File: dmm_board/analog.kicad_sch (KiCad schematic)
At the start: 8 parts

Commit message: work with input prot
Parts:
- removed NT?: NetTie_2, symbol Device:NetTie_2
- added J?: Conn_01x04, symbol Connector_Generic:Conn_01x04
- added NT?: NetTie_2, symbol Device:NetTie_2
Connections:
- net GND: now also C?.2, C?.2, C?.2, NT?.1
- net GNDA: now also NT?.2
- no-connect marks 0 -> 6
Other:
- added sheet current_input (current_input.kicad_sch)
- note added: "v+ mA/uA A com"
- moved on the sheet: C?, U?

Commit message: stuff
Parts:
- added C?: 100n, Capacitor_SMD:C_0603_1608Metric_Pad1.08x0.95mm_HandSolder, symbol Device:C
- added U?: MAX4239AUT, Package_TO_SOT_SMD:SOT-23-6, symbol Amplifier_Operational:MAX4239AUT
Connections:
- new net +2V5: C?.1, U?.5 (~{SHDN}), U?.6 (V+)
- new net -2V5: C?.2
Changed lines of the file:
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@@
   (junction (at 193.04 47.625) (diameter 0) (color 0 0 0 0)
   )
+  (junction (at 123.19 92.075) (diameter 0) (color 0 0 0 0)
+  )
   (junction (at 236.22 47.625) (diameter 0) (color 0 0 0 0)
+  )
+  (junction (at 123.19 82.55) (diameter 0) (color 0 0 0 0)
   )
   (no_connect (at 238.125 65.405))
@@
     (stroke (width 0) (type default) (color 0 0 0 0))
   )
+  (wire (pts (xy 125.73 108.585) (xy 145.415 108.585))
+    (stroke (width 0) (type default) (color 0 0 0 0))
+  )
+  (wire (pts (xy 123.19 82.55) (xy 123.19 92.075))
+    (stroke (width 0) (type default) (color 0 0 0 0))
+  )
   (wire (pts (xy 222.885 102.87) (xy 222.885 100.965))
     (stroke (width 0) (type default) (color 0 0 0 0))
@@
     (stroke (width 0) (type default) (color 0 0 0 0))
   )
+  (wire (pts (xy 145.415 92.075) (xy 123.19 92.075))
+    (stroke (width 0) (type default) (color 0 0 0 0))
+  )
   (wire (pts (xy 193.04 47.625) (xy 193.04 48.26))
     (stroke (width 0) (type default) (color 0 0 0 0))
@@
     (stroke (width 0) (type default) (color 0 0 0 0))
   )
+  (wire (pts (xy 114.3 82.55) (xy 123.19 82.55))
+    (stroke (width 0) (type default) (color 0 0 0 0))
+  )
+  (wire (pts (xy 114.3 83.185) (xy 114.3 82.55))
+    (stroke (width 0) (type default) (color 0 0 0 0))
+  )
   (wire (pts (xy 227.33 38.1) (xy 227.33 39.37))
     (stroke (width 0) (type default) (color 0 0 0 0))
@@
     (stroke (width 0) (type default) (color 0 0 0 0))
   )
+  (wire (pts (xy 123.19 92.075) (xy 123.19 93.345))
+    (stroke (width 0) (type default) (color 0 0 0 0))
+  )
   (wire (pts (xy 203.2 38.1) (xy 212.09 38.1))
     (stroke (width 0) (type default) (color 0 0 0 0))
@@
     (stroke (width 0) (type default) (color 0 0 0 0))
   )
+  (wire (pts (xy 114.3 92.075) (xy 114.3 90.805))
+    (stroke (width 0) (type default) (color 0 0 0 0))
+  )
   (wire (pts (xy 212.09 46.99) (xy 212.09 47.625))
     (stroke (width 0) (type default) (color 0 0 0 0))
@@
     (stroke (width 0) (type default) (color 0 0 0 0))
   )
+  (wire (pts (xy 123.19 81.915) (xy 123.19 82.55))
+    (stroke (width 0) (type default) (color 0 0 0 0))
+  )
   (wire (pts (xy 227.33 47.625) (xy 227.33 46.99))
     (stroke (width 0) (type default) (color 0 0 0 0))
@@
   )
   (wire (pts (xy 222.885 81.915) (xy 222.885 88.9))
+    (stroke (width 0) (type default) (color 0 0 0 0))
+  )
+  (wire (pts (xy 145.415 108.585) (xy 145.415 92.075))
     (stroke (width 0) (type default) (color 0 0 0 0))
   )
@@
     )
     (property "Datasheet" "" (id 3) (at 217.805 88.9 0)
+      (effects (font (size 1.27 1.27)) hide)
+    )
+    (pin "1")
+  )
+  (symbol (lib_id "power:-2V5") (at 114.3 92.075 180) (unit 1)
+    (in_bom yes) (on_board yes) (fields_autoplaced)
+    (property "Reference" "#PWR?" (id 0) (at 114.3 94.615 0)
+      (effects (font (size 1.27 1.27)) hide)
+    )
+    (property "Value" "-2V5" (id 1) (at 115.697 93.824 0)
+      (effects (font (size 1.27 1.27)) (justify right))
+    )
+    (property "Footprint" "" (id 2) (at 114.3 92.075 0)
+      (effects (font (size 1.27 1.27)) hide)
+    )
+    (property "Datasheet" "" (id 3) (at 114.3 92.075 0)
       (effects (font (size 1.27 1.27)) hide)
     )
@@
     (pin "1")
   )
+  (symbol (lib_id "power:-2V5") (at 123.19 112.395 180) (unit 1)
+    (in_bom yes) (on_board yes) (fields_autoplaced)
+    (property "Reference" "#PWR?" (id 0) (at 123.19 114.935 0)
+      (effects (font (size 1.27 1.27)) hide)
+    )
+    (property "Value" "-2V5" (id 1) (at 124.587 114.144 0)
+      (effects (font (size 1.27 1.27)) (justify right))
+    )
+    (property "Footprint" "" (id 2) (at 123.19 112.395 0)
+      (effects (font (size 1.27 1.27)) hide)
+    )
+    (property "Datasheet" "" (id 3) (at 123.19 112.395 0)
+      (effects (font (size 1.27 1.27)) hide)
+    )
+    (pin "1")
+  )
   (symbol (lib_id "Device:C") (at 244.475 43.18 0) (unit 1)
     (in_bom yes) (on_board yes) (fields_autoplaced)
@@
     )
     (property "Datasheet" "" (id 3) (at 222.885 102.87 0)
+      (effects (font (size 1.27 1.27)) hide)
+    )
+    (pin "1")
+  )
+  (symbol (lib_id "power:+2V5") (at 123.19 81.915 0) (unit 1)
+    (in_bom yes) (on_board yes) (fields_autoplaced)
+    (property "Reference" "#PWR?" (id 0) (at 123.19 85.725 0)
+      (effects (font (size 1.27 1.27)) hide)
+    )
+    (property "Value" "+2V5" (id 1) (at 123.19 78.3105 0))
+    (property "Footprint" "" (id 2) (at 123.19 81.915 0)
+      (effects (font (size 1.27 1.27)) hide)
+    )
+    (property "Datasheet" "" (id 3) (at 123.19 81.915 0)
       (effects (font (size 1.27 1.27)) hide)
     )
@@
     (pin "2")
   )
+  (symbol (lib_id "Device:C") (at 114.3 86.995 0) (unit 1)
+    (in_bom yes) (on_board yes) (fields_autoplaced)
+    (property "Reference" "C?" (id 0) (at 117.221 86.0865 0)
+      (effects (font (size 1.27 1.27)) (justify left))
+    )
+    (property "Value" "100n" (id 1) (at 117.221 88.8616 0)
+      (effects (font (size 1.27 1.27)) (justify left))
+    )
+    (property "Footprint" "Capacitor_SMD:C_0603_1608Metric_Pad1.08x0.95mm_HandSolder" (id 2) (at 115.2652 90.805 0)
+      (effects (font (size 1.27 1.27)) hide)
+    )
+    (property "Datasheet" "~" (id 3) (at 114.3 86.995 0)
+      (effects (font (size 1.27 1.27)) hide)
+    )
+    (pin "1")
+    (pin "2")
+  )
   (symbol (lib_id "power:GND") (at 193.04 48.26 0) (unit 1)
     (in_bom yes) (on_board yes) (fields_autoplaced)
@@
     (pin "2")
   )
+  (symbol (lib_id "Amplifier_Operational:MAX4239AUT") (at 125.73 100.965 0) (unit 1)
+    (in_bom yes) (on_board yes) (fields_autoplaced)
+    (property "Reference" "U?" (id 0) (at 137.6385 96.8715 0))
+    (property "Value" "MAX4239AUT" (id 1) (at 137.6385 99.6466 0))
+    (property "Footprint" "Package_TO_SOT_SMD:SOT-23-6" (id 2) (at 125.73 100.965 0)
+      (effects (font (size 1.27 1.27)) hide)
+    )
+    (property "Datasheet" "http://datasheets.maximintegrated.com/en/ds/MAX4238-MAX4239.pdf" (id 3) (at 129.54 97.155 0)
+      (effects (font (size 1.27 1.27)) hide)
+    )
+    (pin "1")
+    (pin "2")
+    (pin "3")
+    (pin "4")
+    (pin "5")
+    (pin "6")
+  )
   (symbol (lib_id "Device:C") (at 203.2 43.18 0) (unit 1)

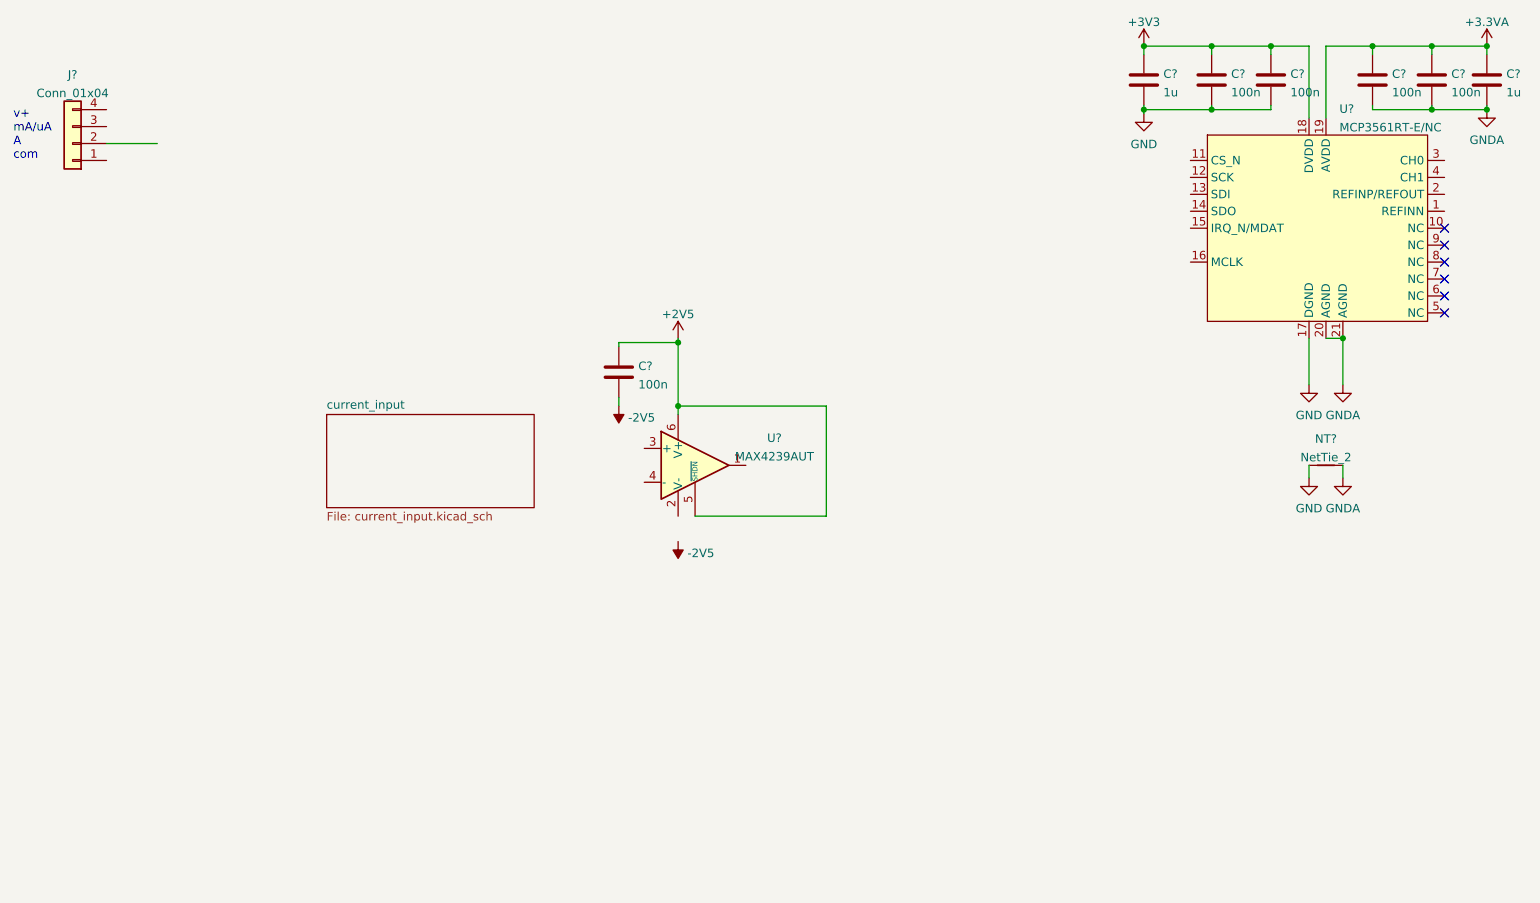
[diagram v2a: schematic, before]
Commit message: more analog input work
need new amp for current -8 instead of -9 that
-8 is unity gain stable -9 is not
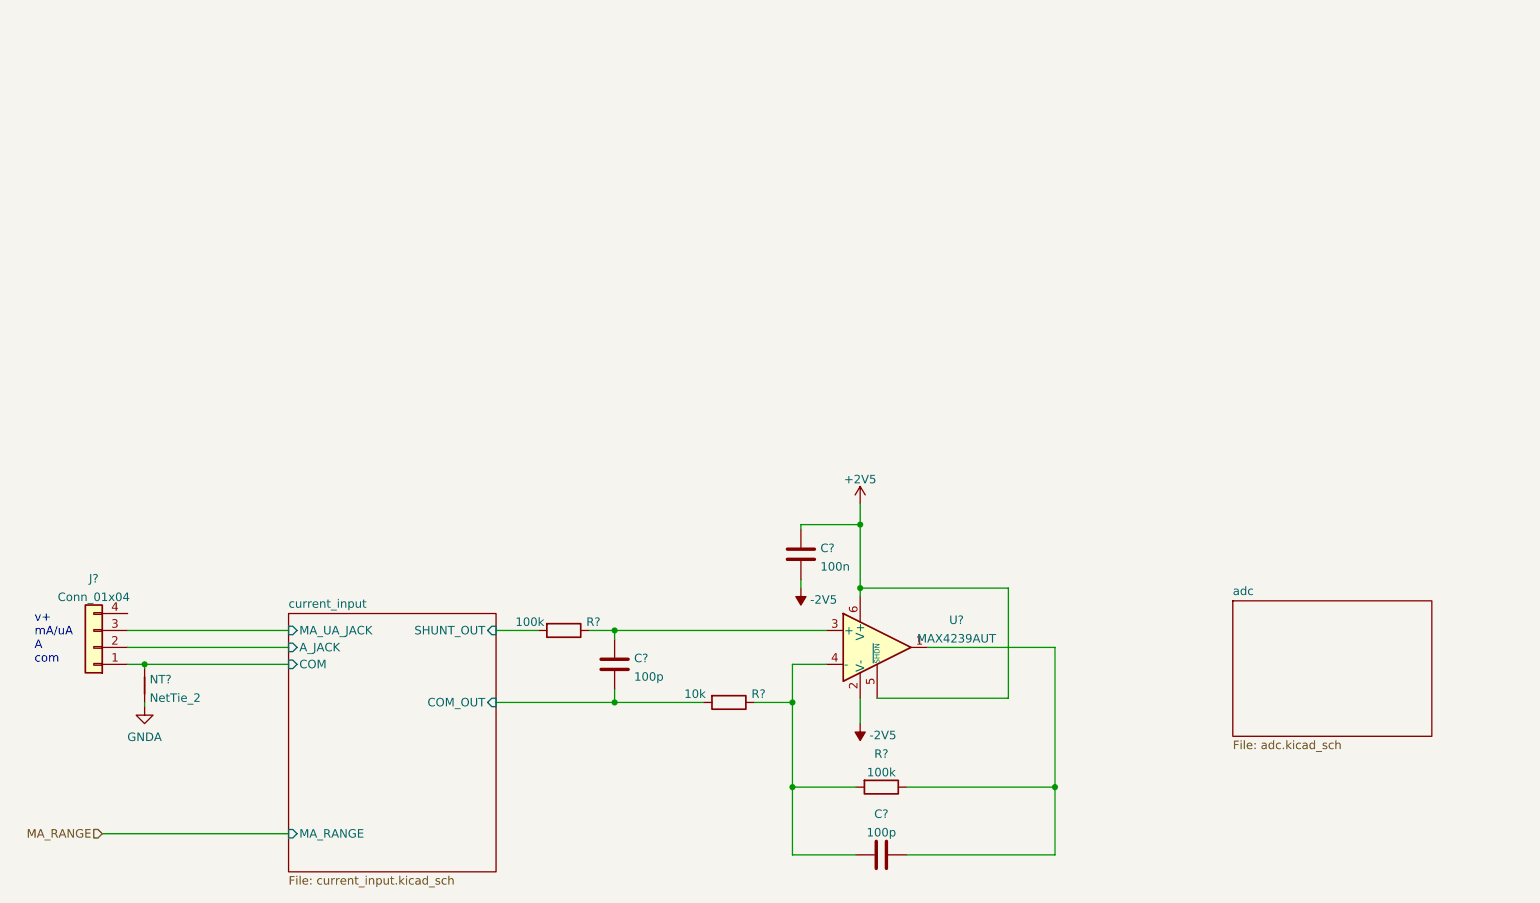
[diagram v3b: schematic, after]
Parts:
- removed C? (x4): 100n, Capacitor_SMD:C_0603_1608Metric_Pad1.08x0.95mm_HandSolder, symbol Device:C
- removed C? (x2): 1u, Capacitor_SMD:C_0603_1608Metric_Pad1.08x0.95mm_HandSolder, symbol Device:C
- removed NT?: NetTie_2, symbol Device:NetTie_2
- removed U?: MCP3561RT-E/NC, Package_DFN_QFN:QFN-20-1EP_3x3mm_P0.4mm_EP1.65x1.65mm_ThermalVias, symbol good_things:MCP3561RT-E/NC
- added C? (x2): 100p, symbol Device:C
- added NT?: NetTie_2, symbol Device:NetTie_2
- added R?: 10k, symbol Device:R
- added R? (x2): 100k, symbol Device:R
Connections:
- net -2V5: now also U?.2 (V-)
- net GNDA: now also NT?.2
- net current_input/COM: now reaches J?.1 (Pin_1)
- net current_input/COM: now also NT?.1
- net current_input/A_JACK: now reaches J?.2 (Pin_2)
- net current_input/MA_UA_JACK: now reaches J?.3 (Pin_3)
- net at U?.1: now also C?.2, R?.1
- net at U?.3 (+): now also C?.2, R?.1
- net at U?.4 (-): now also C?.1, R?.1, R?.2
- new net current_input/COM_OUT: C?.1, R?.2
- new net current_input/SHUNT_OUT: R?.2
- no-connect marks 6 -> 0
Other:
- added sheet adc (adc.kicad_sch)
- sheet current_input ports: added A_JACK, COM, COM_OUT, MA_RANGE, MA_UA_JACK, SHUNT_OUT; removed none
- moved on the sheet: C?, J?, U?
